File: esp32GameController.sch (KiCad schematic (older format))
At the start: 25 parts, among them IC1 BQ21040DBVT, IC2 ESP-WROOM-32_(16MB), J1 USB_B_Micro, J2 Conn_01x02_Male, J3 Conn_02x06_Odd_Even, Q1 2N2219, Q2 2N2219, U1 WIICHUCK, U2 TPS62202DBV

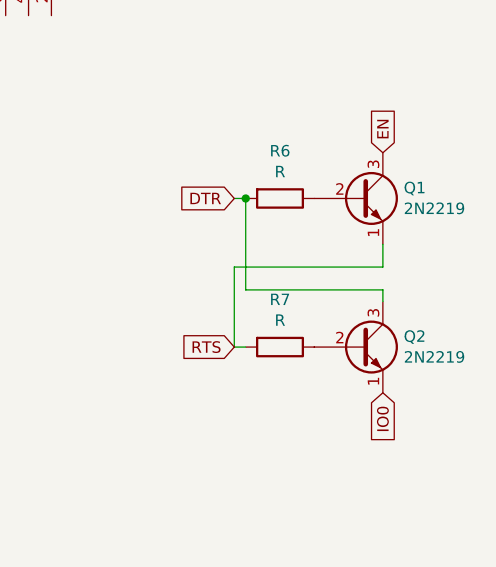
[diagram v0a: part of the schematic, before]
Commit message: Updated footprint and pinouts
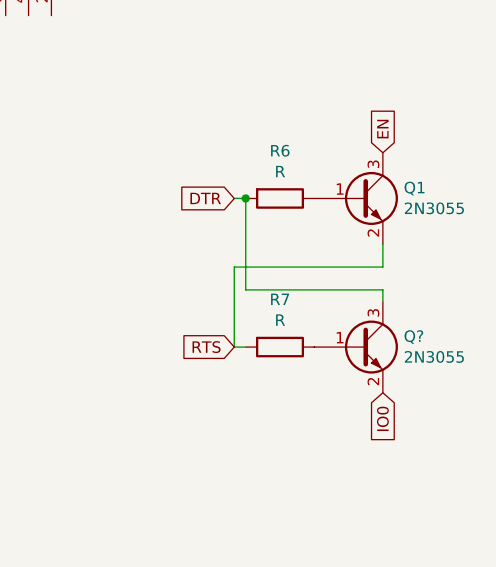
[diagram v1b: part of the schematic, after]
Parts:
- removed Q1, Q2: 2N2219, Package_TO_SOT_SMD:SOT-23, symbol Transistor_BJT:2N2219
- added Q1, Q?: 2N3055, Package_TO_SOT_SMD:SOT-23, symbol Transistor_BJT:2N3055
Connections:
- net DTR: now also Q?.3 (C)
- net EN: now also Q1.3 (C)
- net IO0: now also Q?.2 (E)
- net RTS: now also Q1.2 (E)
- net at R6.1: now also Q1.1 (B)
- net at R7.1: now also Q?.1 (B)
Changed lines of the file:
@@
 EESchema Schematic File Version 4
+LIBS:esp32GameController-cache
 EELAYER 26 0
 EELAYER END
@@
 Connection ~ 5800 2250
 $Comp
-L Transistor_BJT:2N2219 Q2
-U 1 1 5C8E7434
-P 10650 2950
-F 0 "Q2" H 10841 2996 50  0000 L CNN
-F 1 "2N2219" H 10841 2905 50  0000 L CNN
-F 2 "Package_TO_SOT_SMD:SOT-23" H 10850 2875 50  0001 L CIN
-F 3 "http://www.onsemi.com/pub_link/Collateral/2N2219-D.PDF" H 10650 2950 50  0001 L CNN
-	1    10650 2950
-	1    0    0    -1
-$EndComp
-$Comp
 L Connector_Generic:Conn_02x06_Odd_Even J3
 U 1 1 5C8E861B
@@
 	10750 2700 10750 2750
 Connection ~ 10150 2300
-$Comp
-L Transistor_BJT:2N2219 Q1
-U 1 1 5C8E73F2
-P 10650 2300
-F 0 "Q1" H 10841 2346 50  0000 L CNN
-F 1 "2N2219" H 10841 2255 50  0000 L CNN
-F 2 "Package_TO_SOT_SMD:SOT-23" H 10850 2225 50  0001 L CIN
-F 3 "http://www.onsemi.com/pub_link/Collateral/2N2219-D.PDF" H 10650 2300 50  0001 L CNN
-	1    10650 2300
-	1    0    0    -1
-$EndComp
-Wire Wire Line
-	10750 2600 10750 2500
 Wire Wire Line
 	10100 2600 10750 2600
@@
 Text GLabel 7750 2550 2    50   Input ~ 0
 IO0
+Wire Wire Line
+	10750 2500 10750 2600
+$Comp
+L Transistor_BJT:2N3055 Q1
+U 1 1 5C8FA7AB
+P 10650 2300
+F 0 "Q1" H 10841 2346 50  0000 L CNN
+F 1 "2N3055" H 10841 2255 50  0000 L CNN
+F 2 "Package_TO_SOT_SMD:SOT-23" H 10850 2225 50  0001 L CIN
+F 3 "http://www.onsemi.com/pub_link/Collateral/2N3055-D.PDF" H 10650 2300 50  0001 L CNN
+	1    10650 2300
+	1    0    0    -1
+$EndComp
+$Comp
+L Transistor_BJT:2N3055 Q?
+U 1 1 5C8FB335
+P 10650 2950
+F 0 "Q?" H 10841 2996 50  0000 L CNN
+F 1 "2N3055" H 10841 2905 50  0000 L CNN
+F 2 "Package_TO_SOT_SMD:SOT-23" H 10850 2875 50  0001 L CIN
+F 3 "http://www.onsemi.com/pub_link/Collateral/2N3055-D.PDF" H 10650 2950 50  0001 L CNN
+	1    10650 2950
+	1    0    0    -1
+$EndComp
 $EndSCHEMATC

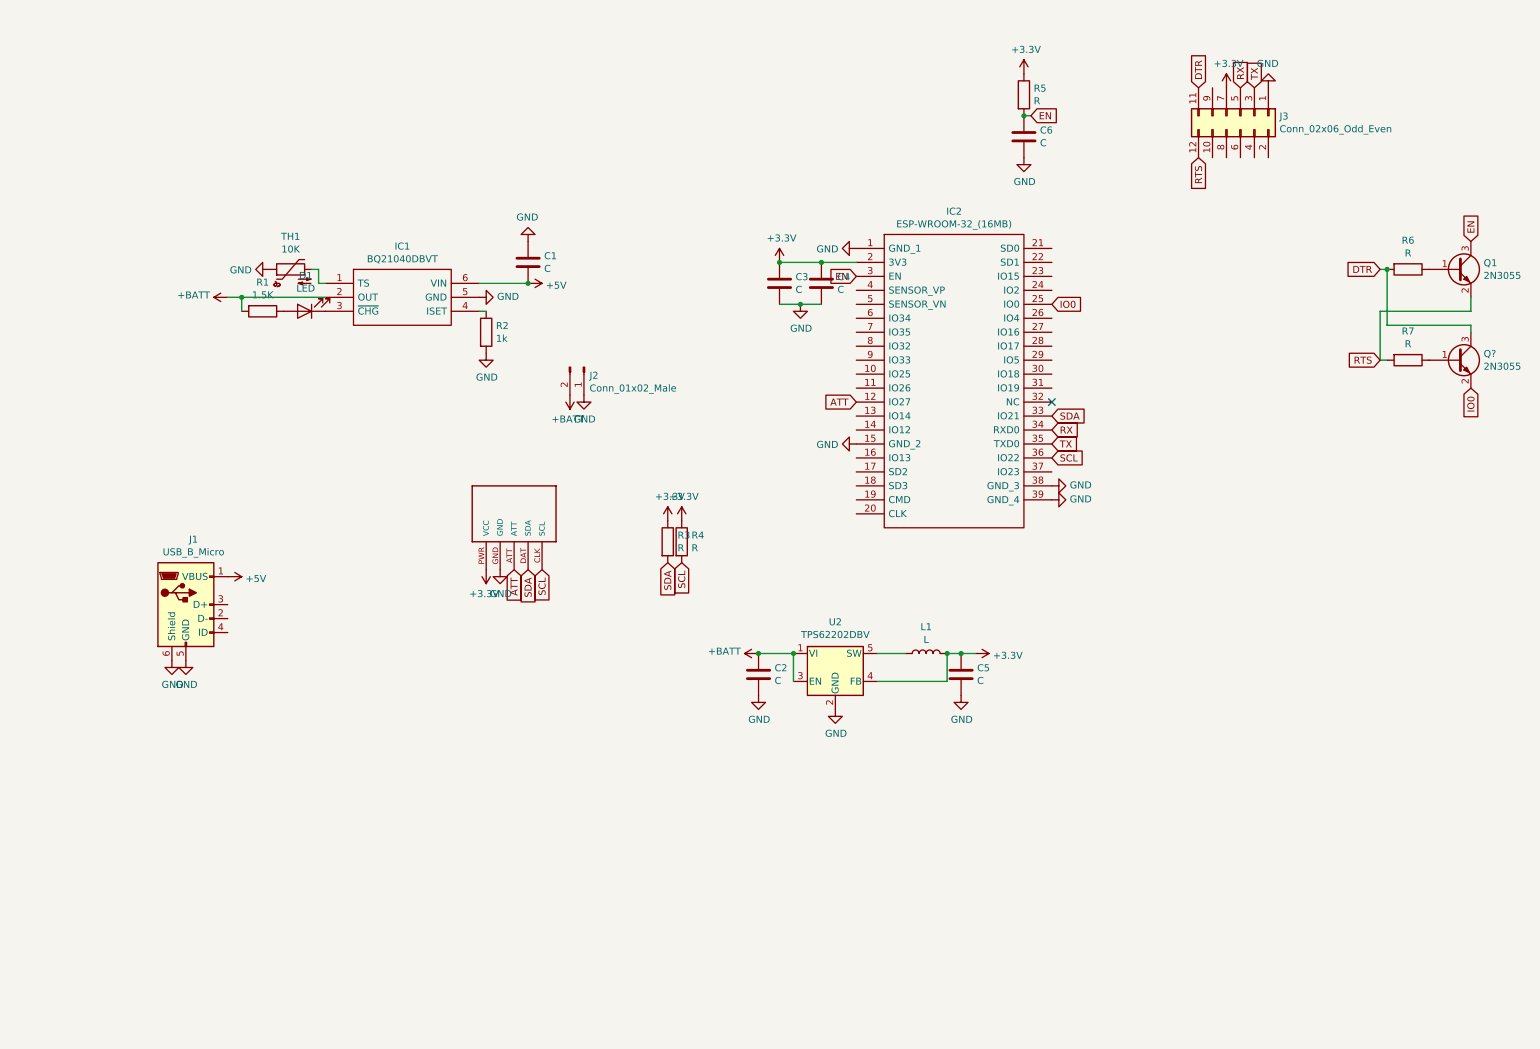
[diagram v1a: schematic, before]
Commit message: Updated schematic to make it easier to read
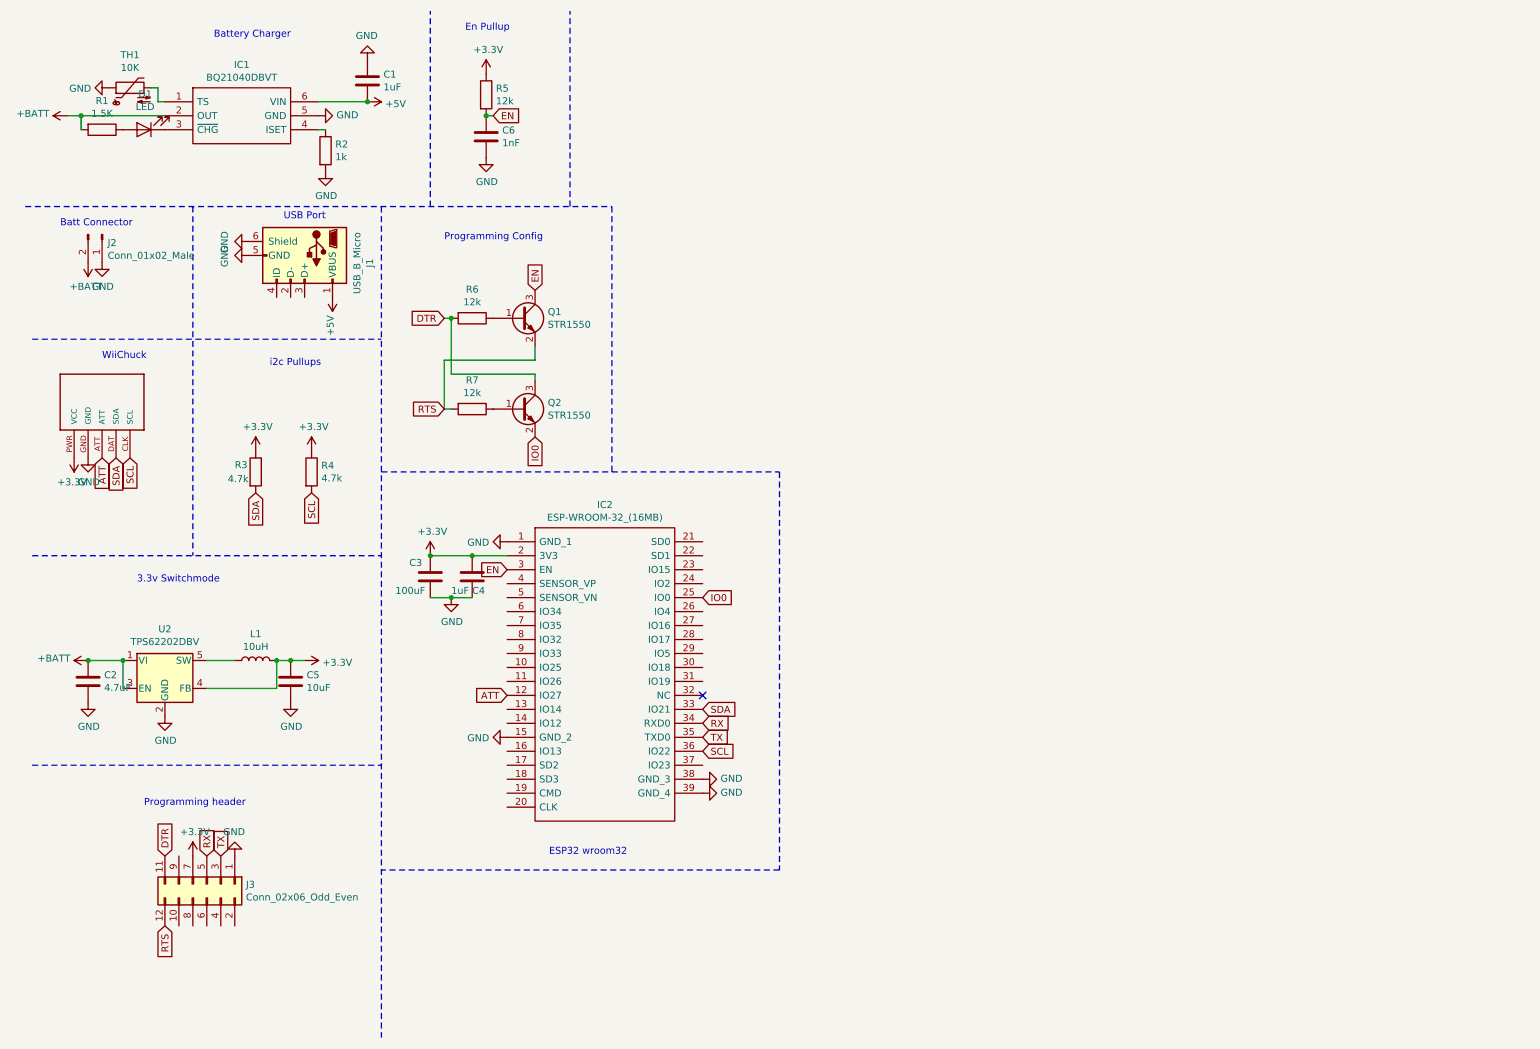
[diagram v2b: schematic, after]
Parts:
- C1, C4: value C -> 1uF
- C2: value C -> 4.7uF
- C3: value C -> 100uF
- C5: value C -> 10uF
- C6: value C -> 1nF
- L1: value L -> 10uH
- Q1: value 2N3055 -> STR1550
- Q2: renamed from Q?; value 2N3055 -> STR1550
- R3, R4: value R -> 4.7k
- R5, R6, R7: value R -> 12k
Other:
- note added: "3.3v Switchmode"
- note added: "Batt Connector"
- note added: "Battery Charger"
- note added: "ESP32 wroom32"
- note added: "En Pullup"
- note added: "Programming Config"
- note added: "Programming header\n"
- note added: "USB Port"
- note added: "WiiChuck"
- note added: "i2c Pullups"
- moved on the sheet: C1, C2, C3, C4, C5, C6, D1, IC1, IC2, J1, J2, J3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
